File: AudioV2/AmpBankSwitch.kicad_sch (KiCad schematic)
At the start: 19 parts, among them U311 TMUX7612, U312 TMUX7612

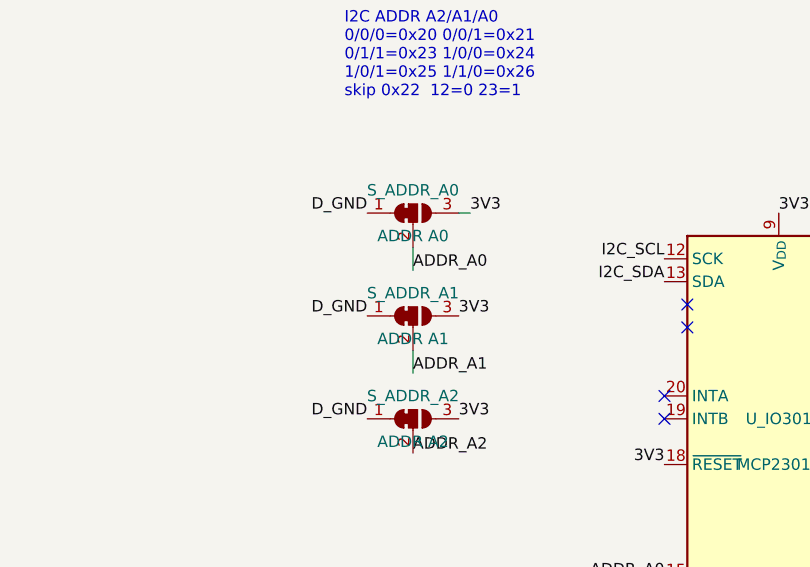
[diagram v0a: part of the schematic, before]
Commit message: AudioV2: Switch の MCP／S_ADDR も build_daughter で生成する
再生成で Switch の ADDR／MCP が消えないように両版をスクリプトに載せ、娘を再生成した。

Co-authored-by: Cursor <cursoragent@cursor.com>
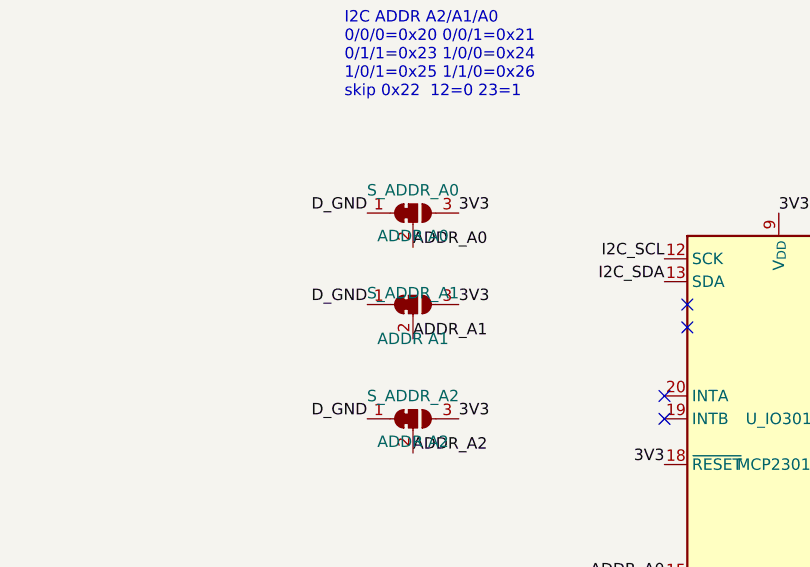
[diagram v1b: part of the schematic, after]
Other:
- moved on the sheet: S_ADDR_A1
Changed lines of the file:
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@@
 	(generator_version "10.0")
 	(paper "A2")
-	(text "I2C ADDR A2/A1/A0
-0/0/0=0x20 0/0/1=0x21
-0/1/1=0x23 1/0/0=0x24
-1/0/1=0x25 1/1/0=0x26
-skip 0x22  12=0 23=1"
+	(text "I2C ADDR A2/A1/A0\n0/0/0=0x20 0/0/1=0x21\n0/1/1=0x23 1/0/0=0x24\n1/0/1=0x25 1/1/0=0x26\nskip 0x22  12=0 23=1"
 		(exclude_from_sim no)
 		(at 152.4 175.26 0)
@@
 	)
 	(no_connect
-		(at 213.36 208.28)
+		(at 213.36 198.12)
 	)
 	(no_connect
@@
 	)
 	(no_connect
-		(at 213.36 193.04)
+		(at 213.36 203.2)
 	)
 	(no_connect
@@
 	)
 	(no_connect
-		(at 213.36 195.58)
+		(at 213.36 205.74)
 	)
 	(no_connect
@@
 	)
 	(no_connect
-		(at 213.36 203.2)
+		(at 213.36 193.04)
 	)
 	(no_connect
@@
 	)
 	(no_connect
-		(at 213.36 200.66)
+		(at 213.36 210.82)
 	)
 	(no_connect
@@
 	)
 	(no_connect
-		(at 213.36 198.12)
+		(at 213.36 208.28)
 	)
 	(no_connect
@@
 	)
 	(no_connect
-		(at 213.36 210.82)
+		(at 213.36 200.66)
 	)
 	(no_connect
-		(at 213.36 205.74)
-	)
-	(wire
-		(pts
-			(xy 160.02 191.77) (xy 160.02 194.31)
-		)
-		(stroke
-			(width 0)
-			(type default)
-		)
-	)
-	(wire
-		(pts
-			(xy 165.1 187.96) (xy 166.37 187.96)
-		)
-		(stroke
-			(width 0)
-			(type default)
-		)
-	)
-	(wire
-		(pts
-			(xy 160.02 205.74) (xy 160.02 203.2)
-		)
-		(stroke
-			(width 0)
-			(type default)
-		)
+		(at 213.36 195.58)
 	)
 	(label "A_GND"
@@
 	)
 	(label "ADDR_A0"
-		(at 160.02 194.31 0)
+		(at 160.02 191.77 0)
 		(effects
 			(font
@@
 	)
 	(label "3V3"
-		(at 166.37 187.96 0)
+		(at 165.1 187.96 0)
 		(effects
 			(font
@@
 	)
 	(label "D_GND"
-		(at 154.94 199.39 180)
+		(at 154.94 198.12 180)
 		(effects
 			(font
@@
 	)
 	(label "3V3"
-		(at 165.1 199.39 0)
+		(at 165.1 198.12 0)
 		(effects
 			(font
@@
 	)
 	(label "ADDR_A1"
-		(at 160.02 205.74 0)
+		(at 160.02 201.93 0)
 		(effects
 			(font
@@
 			)
 		)
-		(property "Description" ""
+		(property "Description" "基板間15mm用ロングテール（約11mm）。母板ソケットと対（A5案a）"
 			(at 0 0 0)
 			(hide yes)
@@
 		)
 		(property "Footprint" "Jumper:SolderJumper-3_P1.3mm_Bridged12_Pad1.0x1.5mm_NumberLabels"
-			(at -50.8 20.32 0)
+			(at 0 0 0)
 			(hide yes)
 			(show_name no)
@@
 		)
 		(property "Datasheet" ""
-			(at -50.8 20.32 0)
+			(at 0 0 0)
 			(hide yes)
 			(show_name no)
@@
 		)
 		(property "Description" ""
-			(at -50.8 20.32 0)
+			(at 0 0 0)
 			(hide yes)
 			(show_name no)
@@
 		)
 		(property "Footprint" "Jumper:SolderJumper-3_P1.3mm_Bridged12_Pad1.0x1.5mm_NumberLabels"
-			(at -10.16 -2.54 0)
+			(at 0 0 0)
 			(hide yes)
 			(show_name no)
@@
 		)
 		(property "Datasheet" ""
-			(at -10.16 -2.54 0)
+			(at 0 0 0)
 			(hide yes)
 			(show_name no)
@@
 		)
 		(property "Description" ""
-			(at -10.16 -2.54 0)
+			(at 0 0 0)
 			(hide yes)
 			(show_name no)
@@
 			)
 		)
-		(property "Description" ""
+		(property "Description" "基板間15mm用ロングテール（約11mm）・金メッキ。母板ソケットと対（A5案a）"
 			(at 0 0 0)
 			(hide yes)
@@
 	(symbol
 		(lib_id "Jumper:SolderJumper_3_Bridged12")
-		(at 160.02 199.39 0)
+		(at 160.02 198.12 0)
 		(unit 1)
 		(body_style 1)
@@
 		)
 		(property "Footprint" "Jumper:SolderJumper-3_P1.3mm_Bridged12_Pad1.0x1.5mm_NumberLabels"
-			(at -30.48 8.89 0)
+			(at 0 0 0)
 			(hide yes)
 			(show_name no)
@@
 		)
 		(property "Datasheet" ""
-			(at -30.48 8.89 0)
+			(at 0 0 0)
 			(hide yes)
 			(show_name no)
@@
 		)
 		(property "Description" ""
-			(at -30.48 8.89 0)
-			(hide yes)
-			(show_name no)
+			(at 0 0 0)
+			(hide yes)
+			(show_name no)

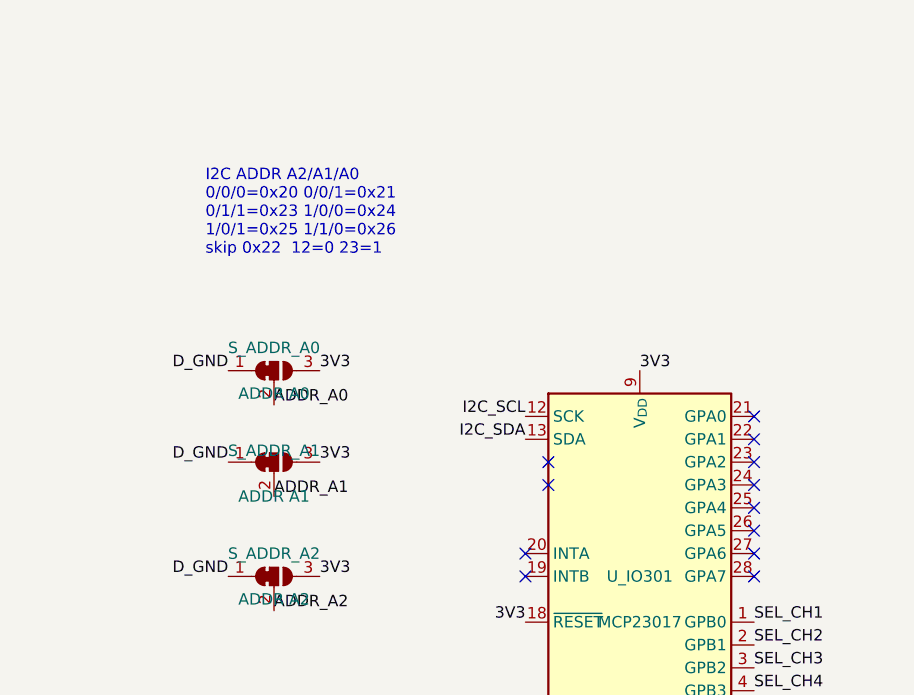
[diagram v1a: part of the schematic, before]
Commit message: AudioV2: 親スロットを ANA/PWR 各1組（101）に減らす
当面は Switch 娘1枚前提。102/103 を回路図と PCB から外した。

Co-authored-by: Cursor <cursoragent@cursor.com>
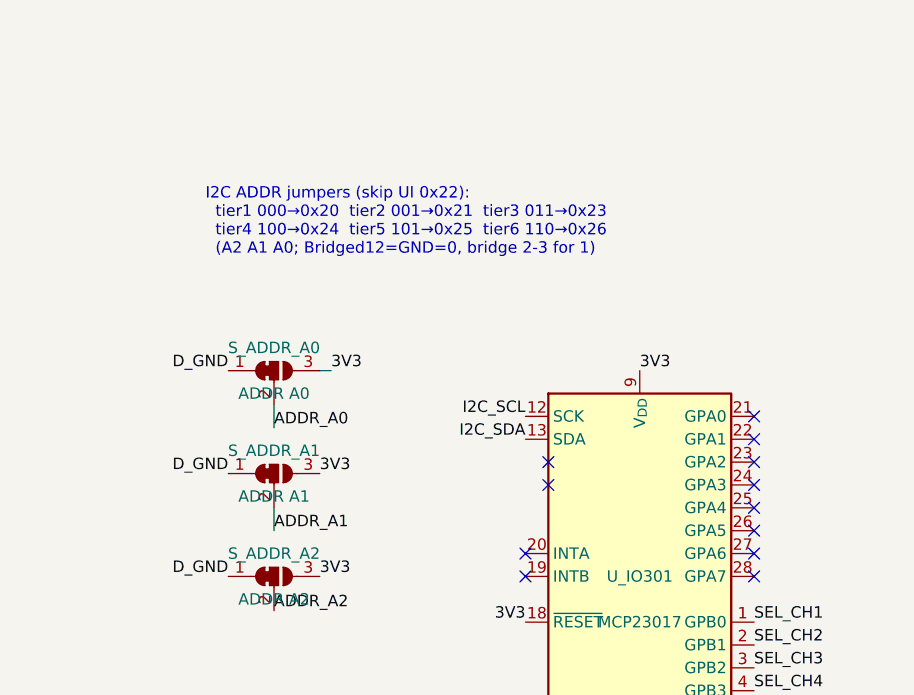
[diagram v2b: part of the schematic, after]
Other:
- note added: "I2C ADDR jumpers (skip UI 0x22): tier1 000→0x20 tier2 001→0x21 tier3 011→0x23 tier4 100→0x24 tier5 101→0x25 tier6 110→0x26 (A2 A1 A0; Bridged12=GND=0, bridge 2-3 for 1)"
- note removed: "I2C ADDR A2/A1/A0 0/0/0=0x20 0/0/1=0x21 0/1/1=0x23 1/0/0=0x24 1/0/1=0x25 1/1/0=0x26 skip 0x22 12=0 23=1"
- moved on the sheet: S_ADDR_A1
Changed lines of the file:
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@@
 	(generator_version "10.0")
 	(paper "A2")
-	(text "I2C ADDR A2/A1/A0\n0/0/0=0x20 0/0/1=0x21\n0/1/1=0x23 1/0/0=0x24\n1/0/1=0x25 1/1/0=0x26\nskip 0x22  12=0 23=1"
+	(text "I2C ADDR jumpers (skip UI 0x22):\n  tier1 000→0x20  tier2 001→0x21  tier3 011→0x23\n  tier4 100→0x24  tier5 101→0x25  tier6 110→0x26\n  (A2 A1 A0; Bridged12=GND=0, bridge 2-3 for 1)"
 		(exclude_from_sim no)
 		(at 152.4 175.26 0)
@@
 	)
 	(no_connect
-		(at 213.36 198.12)
+		(at 213.36 208.28)
 	)
 	(no_connect
@@
 	)
 	(no_connect
-		(at 213.36 203.2)
+		(at 213.36 193.04)
 	)
 	(no_connect
@@
 	)
 	(no_connect
-		(at 213.36 205.74)
+		(at 213.36 195.58)
 	)
 	(no_connect
@@
 	)
 	(no_connect
-		(at 213.36 193.04)
+		(at 213.36 203.2)
 	)
 	(no_connect
@@
 	)
 	(no_connect
-		(at 213.36 210.82)
+		(at 213.36 200.66)
 	)
 	(no_connect
@@
 	)
 	(no_connect
-		(at 213.36 208.28)
+		(at 213.36 198.12)
 	)
 	(no_connect
@@
 	)
 	(no_connect
-		(at 213.36 200.66)
+		(at 213.36 210.82)
 	)
 	(no_connect
-		(at 213.36 195.58)
+		(at 213.36 205.74)
+	)
+	(wire
+		(pts
+			(xy 160.02 191.77) (xy 160.02 194.31)
+		)
+		(stroke
+			(width 0)
+			(type default)
+		)
+	)
+	(wire
+		(pts
+			(xy 165.1 187.96) (xy 166.37 187.96)
+		)
+		(stroke
+			(width 0)
+			(type default)
+		)
+	)
+	(wire
+		(pts
+			(xy 160.02 205.74) (xy 160.02 203.2)
+		)
+		(stroke
+			(width 0)
+			(type default)
+		)
 	)
 	(label "A_GND"
@@
 	)
 	(label "ADDR_A0"
-		(at 160.02 191.77 0)
+		(at 160.02 194.31 0)
 		(effects
 			(font
@@
 	)
 	(label "3V3"
-		(at 165.1 187.96 0)
+		(at 166.37 187.96 0)
 		(effects
 			(font
@@
 	)
 	(label "D_GND"
-		(at 154.94 198.12 180)
+		(at 154.94 199.39 180)
 		(effects
 			(font
@@
 	)
 	(label "3V3"
-		(at 165.1 198.12 0)
+		(at 165.1 199.39 0)
 		(effects
 			(font
@@
 	)
 	(label "ADDR_A1"
-		(at 160.02 201.93 0)
+		(at 160.02 205.74 0)
 		(effects
 			(font
@@
 			)
 		)
-		(property "Description" "基板間15mm用ロングテール（約11mm）。母板ソケットと対（A5案a）"
+		(property "Description" ""
 			(at 0 0 0)
 			(hide yes)
@@
 		)
 		(property "Footprint" "Jumper:SolderJumper-3_P1.3mm_Bridged12_Pad1.0x1.5mm_NumberLabels"
-			(at 0 0 0)
+			(at -50.8 20.32 0)
 			(hide yes)
 			(show_name no)
@@
 		)
 		(property "Datasheet" ""
-			(at 0 0 0)
+			(at -50.8 20.32 0)
 			(hide yes)
 			(show_name no)
@@
 		)
 		(property "Description" ""
-			(at 0 0 0)
+			(at -50.8 20.32 0)
 			(hide yes)
 			(show_name no)
@@
 		)
 		(property "Footprint" "Jumper:SolderJumper-3_P1.3mm_Bridged12_Pad1.0x1.5mm_NumberLabels"
-			(at 0 0 0)
+			(at -10.16 -2.54 0)
 			(hide yes)
 			(show_name no)
@@
 		)
 		(property "Datasheet" ""
-			(at 0 0 0)
+			(at -10.16 -2.54 0)
 			(hide yes)
 			(show_name no)
@@
 		)
 		(property "Description" ""
-			(at 0 0 0)
+			(at -10.16 -2.54 0)
 			(hide yes)
 			(show_name no)
@@
 			)
 		)
-		(property "Description" "基板間15mm用ロングテール（約11mm）・金メッキ。母板ソケットと対（A5案a）"
+		(property "Description" ""
 			(at 0 0 0)
 			(hide yes)
@@
 	(symbol
 		(lib_id "Jumper:SolderJumper_3_Bridged12")
-		(at 160.02 198.12 0)
+		(at 160.02 199.39 0)
 		(unit 1)
 		(body_style 1)
@@
 		)
 		(property "Footprint" "Jumper:SolderJumper-3_P1.3mm_Bridged12_Pad1.0x1.5mm_NumberLabels"
-			(at 0 0 0)
+			(at -30.48 8.89 0)
 			(hide yes)
 			(show_name no)
@@
 		)
 		(property "Datasheet" ""
-			(at 0 0 0)
+			(at -30.48 8.89 0)
 			(hide yes)
 			(show_name no)
@@
 		)
 		(property "Description" ""
-			(at 0 0 0)
-			(hide yes)
-			(show_name no)
+			(at -30.48 8.89 0)
+			(hide yes)
+			(show_name no)

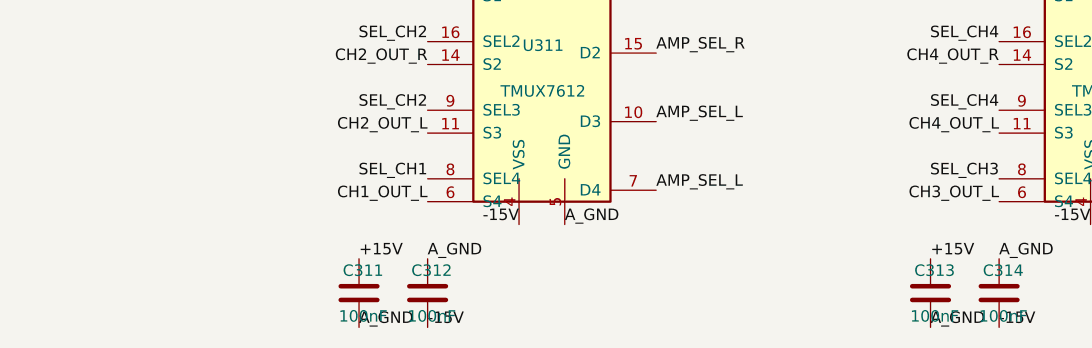
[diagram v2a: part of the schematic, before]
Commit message: AudioV2: TMUX7612 に DS 推奨の 1 µF を追加（AmpBankSwitch、0603 ×4）
DS p34 は VDD/VSS それぞれ 0.1 µF と 1 µF を推奨。DECISIONS 決定済みの追加で、サイズはユーザー指示で 0603。
build_daughter.py に C315–C318（1uF 50V X7R）を足し、fixed_uids() で UUID を通し番号から切り離した
（途中に足すと後ろの UUID が Relay 版まで全部ずれ、PCB との KIID パスが切れるため）。
コミット済みの回路図は手の見た目修正が生成物より新しいので、全面再生成はせず、
新しい生成物から C315–C318 と各ラベルだけを差し込んで正準化した（既存の行は 0 行変化）。
netlist_partition: 既存の分割は完全一致（344 ネット）、足した4個は +15V/-15V/A_GND のみ。ERC は HEAD と同一。

Co-Authored-By: Claude Opus 5.5 <noreply@anthropic.com>
Claude-Session: https://claude.ai/code/session_01NpwAm89hZpJTCZphnQ6odp
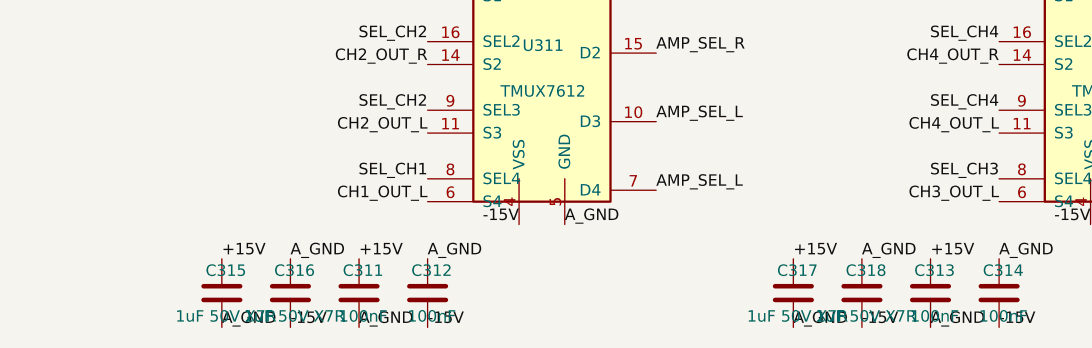
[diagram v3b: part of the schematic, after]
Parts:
- added C315, C316, C317, C318: 1uF 50V X7R, Capacitor_SMD:C_0603_1608Metric_Pad1.08x0.95mm_HandSolder, symbol Device:C
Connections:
- net +15V: now also C315.1, C317.1
- net -15V: now also C316.2, C318.2
- net A_GND: now also C315.2, C316.1, C317.2, C318.1

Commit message: AudioV2: TMUX の 100 nF（C311–C314）を 0603 に（回路図）
ピンの足元（本体直下の裏）へ寄せるためのフットプリント変更。値・ネットは不変。
build_daughter.py と回路図の Footprint 4行だけを差し替え（生成物との差もこの4行のみ、Relay は不変）。

Co-Authored-By: Claude Opus 5.5 <noreply@anthropic.com>
Claude-Session: https://claude.ai/code/session_01NpwAm89hZpJTCZphnQ6odp
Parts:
- C311, C312, C313, C314: footprint Capacitor_SMD:C_1206_3216Metric_Pad1.33x1.80mm_HandSolder -> Capacitor_SMD:C_0603_1608Metric_Pad1.08x0.95mm_HandSolder
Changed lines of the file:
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@@
 			)
 		)
-		(property "Footprint" "Capacitor_SMD:C_1206_3216Metric_Pad1.33x1.80mm_HandSolder"
+		(property "Footprint" "Capacitor_SMD:C_0603_1608Metric_Pad1.08x0.95mm_HandSolder"
 			(at 0 0 0)
 			(hide yes)
@@
 			)
 		)
-		(property "Footprint" "Capacitor_SMD:C_1206_3216Metric_Pad1.33x1.80mm_HandSolder"
+		(property "Footprint" "Capacitor_SMD:C_0603_1608Metric_Pad1.08x0.95mm_HandSolder"
 			(at 0 0 0)
 			(hide yes)
@@
 			)
 		)
-		(property "Footprint" "Capacitor_SMD:C_1206_3216Metric_Pad1.33x1.80mm_HandSolder"
+		(property "Footprint" "Capacitor_SMD:C_0603_1608Metric_Pad1.08x0.95mm_HandSolder"
 			(at 0 0 0)
 			(hide yes)
@@
 			)
 		)
-		(property "Footprint" "Capacitor_SMD:C_1206_3216Metric_Pad1.33x1.80mm_HandSolder"
-			(at 0 0 0)
-			(hide yes)
+		(property "Footprint" "Capacitor_SMD:C_0603_1608Metric_Pad1.08x0.95mm_HandSolder"
+			(at 0 0 0)
+			(hide yes)

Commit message: AudioV2: MCP23017 の 100 nF を 0603 にして VDD/VSS の足の真上（裏）へ（Switch/Relay）
- C_IO301 / C_IO302: 1206 → 0603。電源パッドを pin9 の真上、GND パッドを pin10 の脇に置き、
  両側を約 1.6 mm の裏の線で足へ直結（いままで GND 側は線が無くベタ経由、Relay の 3V3 は 5 mm の斜め線）
- Relay: 置き場所に重なる D_GND ステッチビアを1本外す
- 回路図2枚と build_daughter.py のフットプリントを 0603 に
- swap_to_0603: 旧部品は Delete() で消す（Remove() だと Python ラッパー回収時に SWIG の型表が壊れ、
  以後の FOOTPRINT / PADS が 'SwigPyObject' になる）

DRC: 新規違反 0・未接続不変・schematic parity 0。ERC 5 のまま。PARTS.md 再生成。

Co-Authored-By: Claude Opus 5.5 <noreply@anthropic.com>
Claude-Session: https://claude.ai/code/session_01NpwAm89hZpJTCZphnQ6odp
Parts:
- C_IO301: footprint Capacitor_SMD:C_1206_3216Metric_Pad1.33x1.80mm_HandSolder -> Capacitor_SMD:C_0603_1608Metric_Pad1.08x0.95mm_HandSolder
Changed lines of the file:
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@@
 			)
 		)
-		(property "Footprint" "Capacitor_SMD:C_1206_3216Metric_Pad1.33x1.80mm_HandSolder"
+		(property "Footprint" "Capacitor_SMD:C_0603_1608Metric_Pad1.08x0.95mm_HandSolder"
 			(at 0 0 0)
 			(hide yes)
